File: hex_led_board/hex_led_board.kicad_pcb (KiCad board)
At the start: 2 copper layers, 69.3 x 80 mm, 90 parts, among them J1 Conn_01x04, J2 Conn_01x04

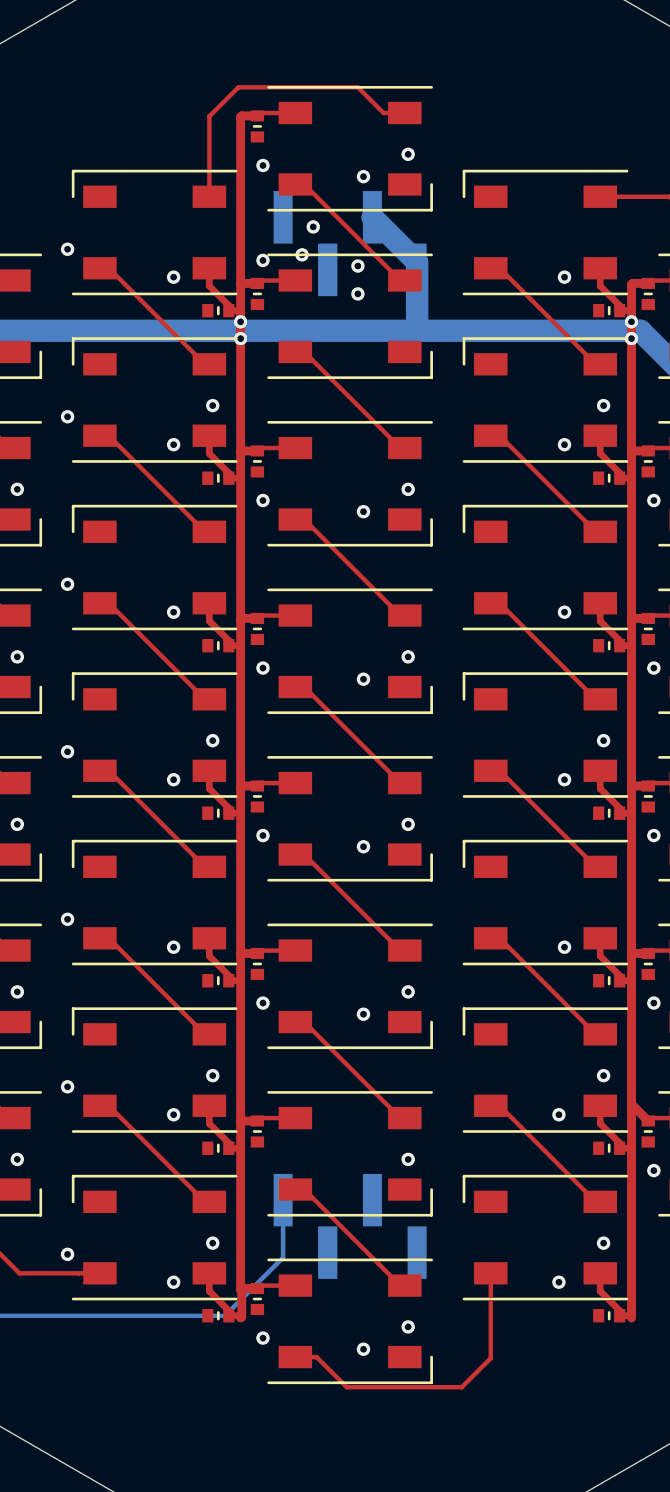
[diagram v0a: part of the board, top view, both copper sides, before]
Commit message: finished led board
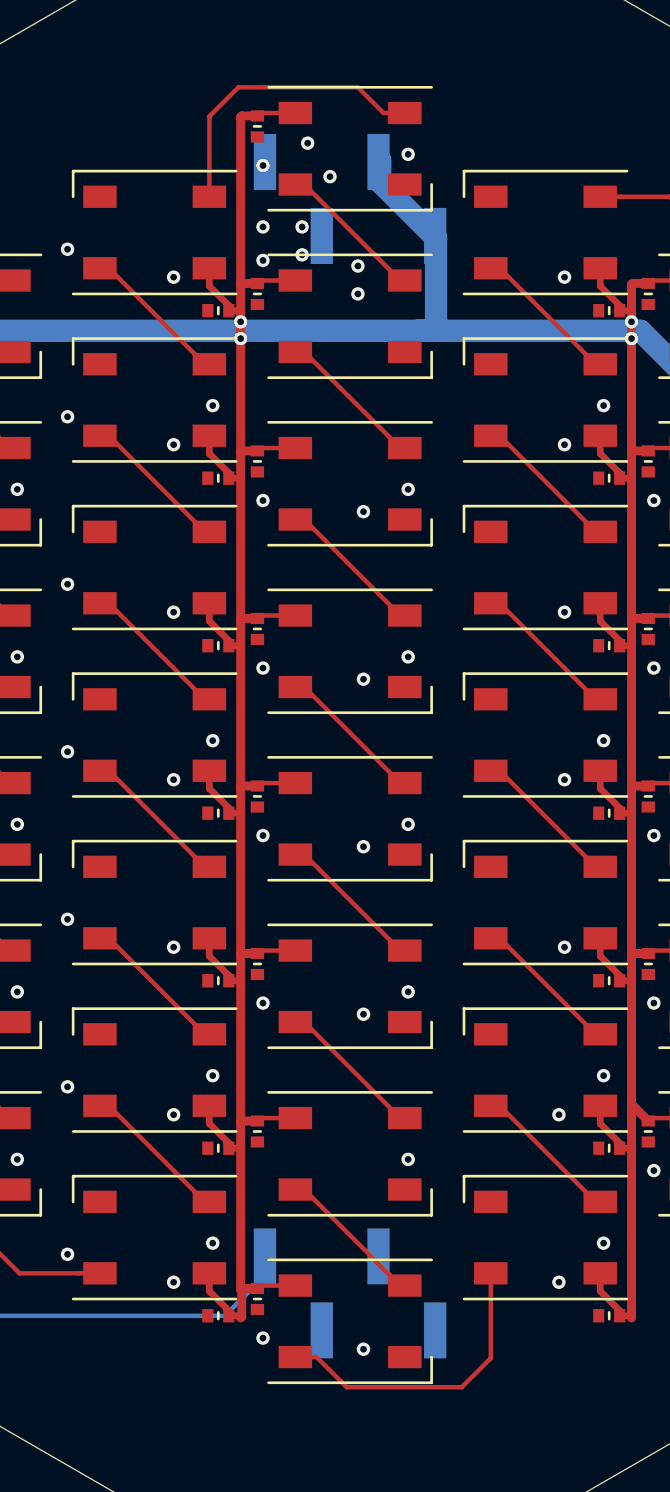
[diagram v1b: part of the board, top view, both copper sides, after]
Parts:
- J1, J2: footprint Connector_PinHeader_2.00mm:PinHeader_1x04_P2.00mm_Vertical_SMD_Pin1Left -> Connector_PinHeader_2.54mm:PinHeader_1x04_P2.54mm_Vertical_SMD_Pin1Left
- moved J2 3.00 mm to (100.0, 125.0)
- moved J1 2.00 mm to (100.0, 76.0)
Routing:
- net VBUS: track 345.0 -> 348.5 mm
- net DIN: track 33.2 -> 30.4 mm
- net GND: vias 109 -> 110
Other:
- board text added: "JLCJLCJLCJLC"
